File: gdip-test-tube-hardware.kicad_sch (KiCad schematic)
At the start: 13 parts, among them J1 USB_B, J2 USB_B, J3 Conn_01x06, J4 Conn_01x06, J5 Conn_01x06, U1 ESP32-S3-WROOM-1-N16R2, U2 AMS1117-3.3, U3 CP2102N-Axx-xQFN28, U4 USBLC6-2SC6, U5 USBLC6-2SC6

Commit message: Added connections for servo and finshed up usb-serial ic.
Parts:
- added C3: 1uF, symbol Device:C
- added C4: 10uF, symbol Device:C
- added R1: 22.1k, symbol Device:R
- added R2: 47.5K, symbol Device:R
- added R3: 1K, symbol Device:R
- added SW1, SW2: SW_Push, symbol Switch:SW_Push
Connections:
- net D2+_OUT: now also U3.4 (D+)
- net D2-_OUT: now also U3.5 (D-)
- net GND: now also U3.29 (GND), U3.3 (GND), C3.2, C4.2, R2.1
- net +3.3V: now reaches U3.6 (VDD)
- net +3.3V: now also U3.7 (VREGIN), C4.1, R3.1
- net at U3.8 (VBUS): now also C3.1, R1.2, R2.2
- net at U3.9 (~{RST}): now also R3.2
- net +5V: now reaches C2.1, J2.1 (VBUS), U5.5 (VBUS)
- net +5V: now also C1.1, J1.1 (VBUS), U4.5 (VBUS), R1.1
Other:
- note added: "BUTTONS"
- moved on the sheet: J3, J4, J5, U3

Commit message: Added auto prog circuit.
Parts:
- added C5: 10uF, symbol Device:C
- added C6: 0.1uF, symbol Device:C
- added J6: Screw_Terminal_01x02, symbol Connector:Screw_Terminal_01x02
- added Q1, Q2: S8050, Package_TO_SOT_THT:TO-92_Inline, symbol Transistor_BJT:S8050
- added R10, R11, R4, R5, R6, R7: 0, symbol Device:R
- added R8, R9: 10k, symbol Device:R
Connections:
- net +3.3V: now also C5.1, C6.1, R7.1
- net +5V: now also J3.1 (Pin_1), J3.2 (Pin_2), J3.3 (Pin_3), J3.4 (Pin_4), J3.5 (Pin_5), J3.6 (Pin_6)
- net GND: now also J5.1 (Pin_1), J5.2 (Pin_2), J5.3 (Pin_3), J5.4 (Pin_4), J5.5 (Pin_5), J5.6 (Pin_6), U1.1 (GND), U1.40 (GND), U1.41_1 (GND), U1.41_2 (GND), U1.41_3 (GND), U1.41_4 (GND), U1.41_5 (GND), U1.41_6 (GND), U1.41_7 (GND), U1.41_8 (GND), U1.41_9 (GND), C5.2, C6.2, R6.1
- net at U3.11 (~{SUSPEND}): now also R6.2
- net RTS: now reaches U3.24 (~{RTS})
- net RTS: now also Q1.1 (E), R9.2
- net at U3.25 (RXD): now also R5.2
- net at U3.26 (TXD): now also R4.2
- net DTR: now reaches U3.28 (~{DTR})
- net DTR: now also Q2.3 (C), R8.2
- net at U1.2 (3V3): now also R7.2
- net U0RXD: now reaches U1.36 (RXD0)
- net U0RXD: now also R4.1
- net U0TXD: now reaches U1.37 (TXD0)
- net U0TXD: now also R5.1
- new net: Q1.2 (B), R8.1
- new net: Q1.3 (C), R10.2
- new net: Q2.1 (E), R11.2
- new net: Q2.2 (B), R9.1
- new net CHIP_PU: R10.1
- new net GPIO0: R11.1
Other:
- note added: "MCU Power (3.3V)"
- note added: "Motor Supply (5V)"
- note added: "Power Pin Headers"
- note added: "USB"
- moved on the sheet: C3, C4, J3, J4, J5, R1, R2, R3, SW1, SW2, U1, U2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

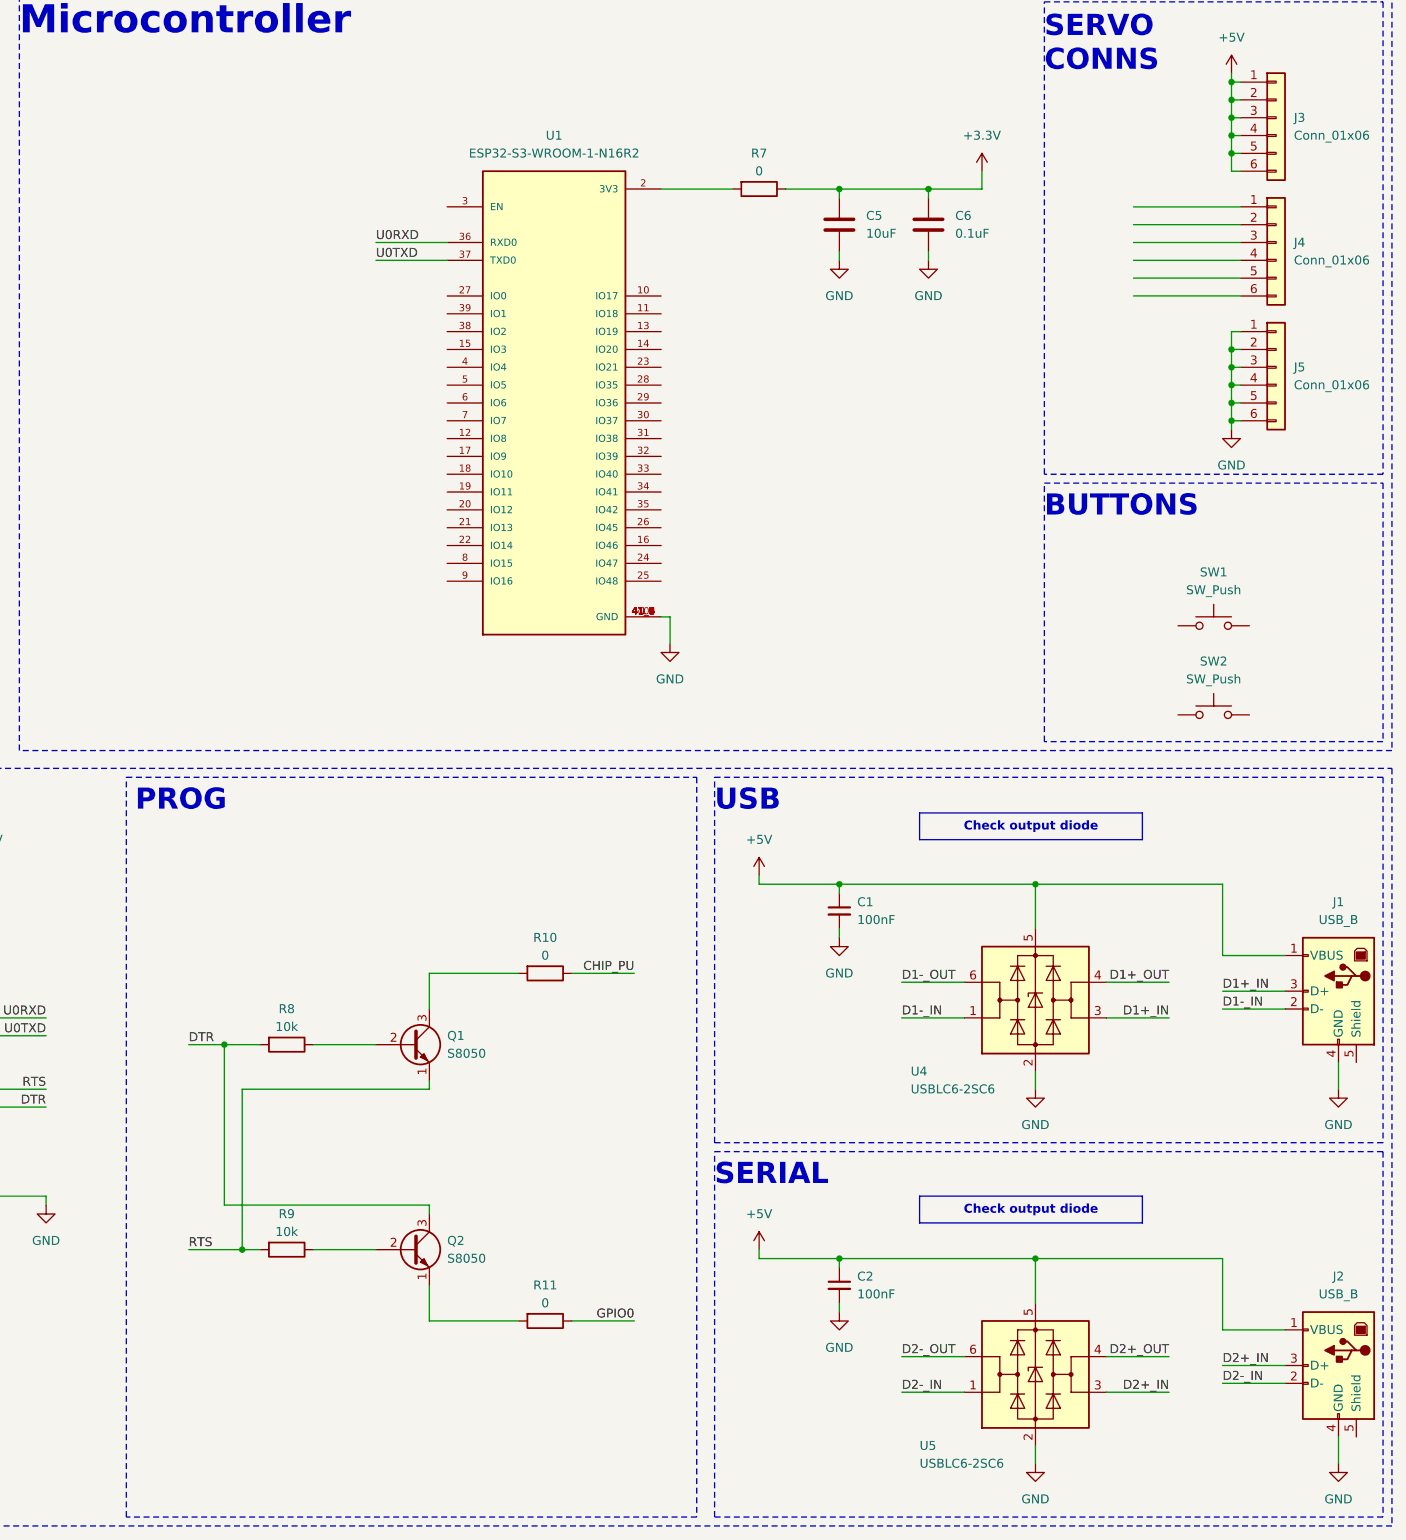
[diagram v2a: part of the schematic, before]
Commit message: Added pinout and connect pwm to servo pin header.
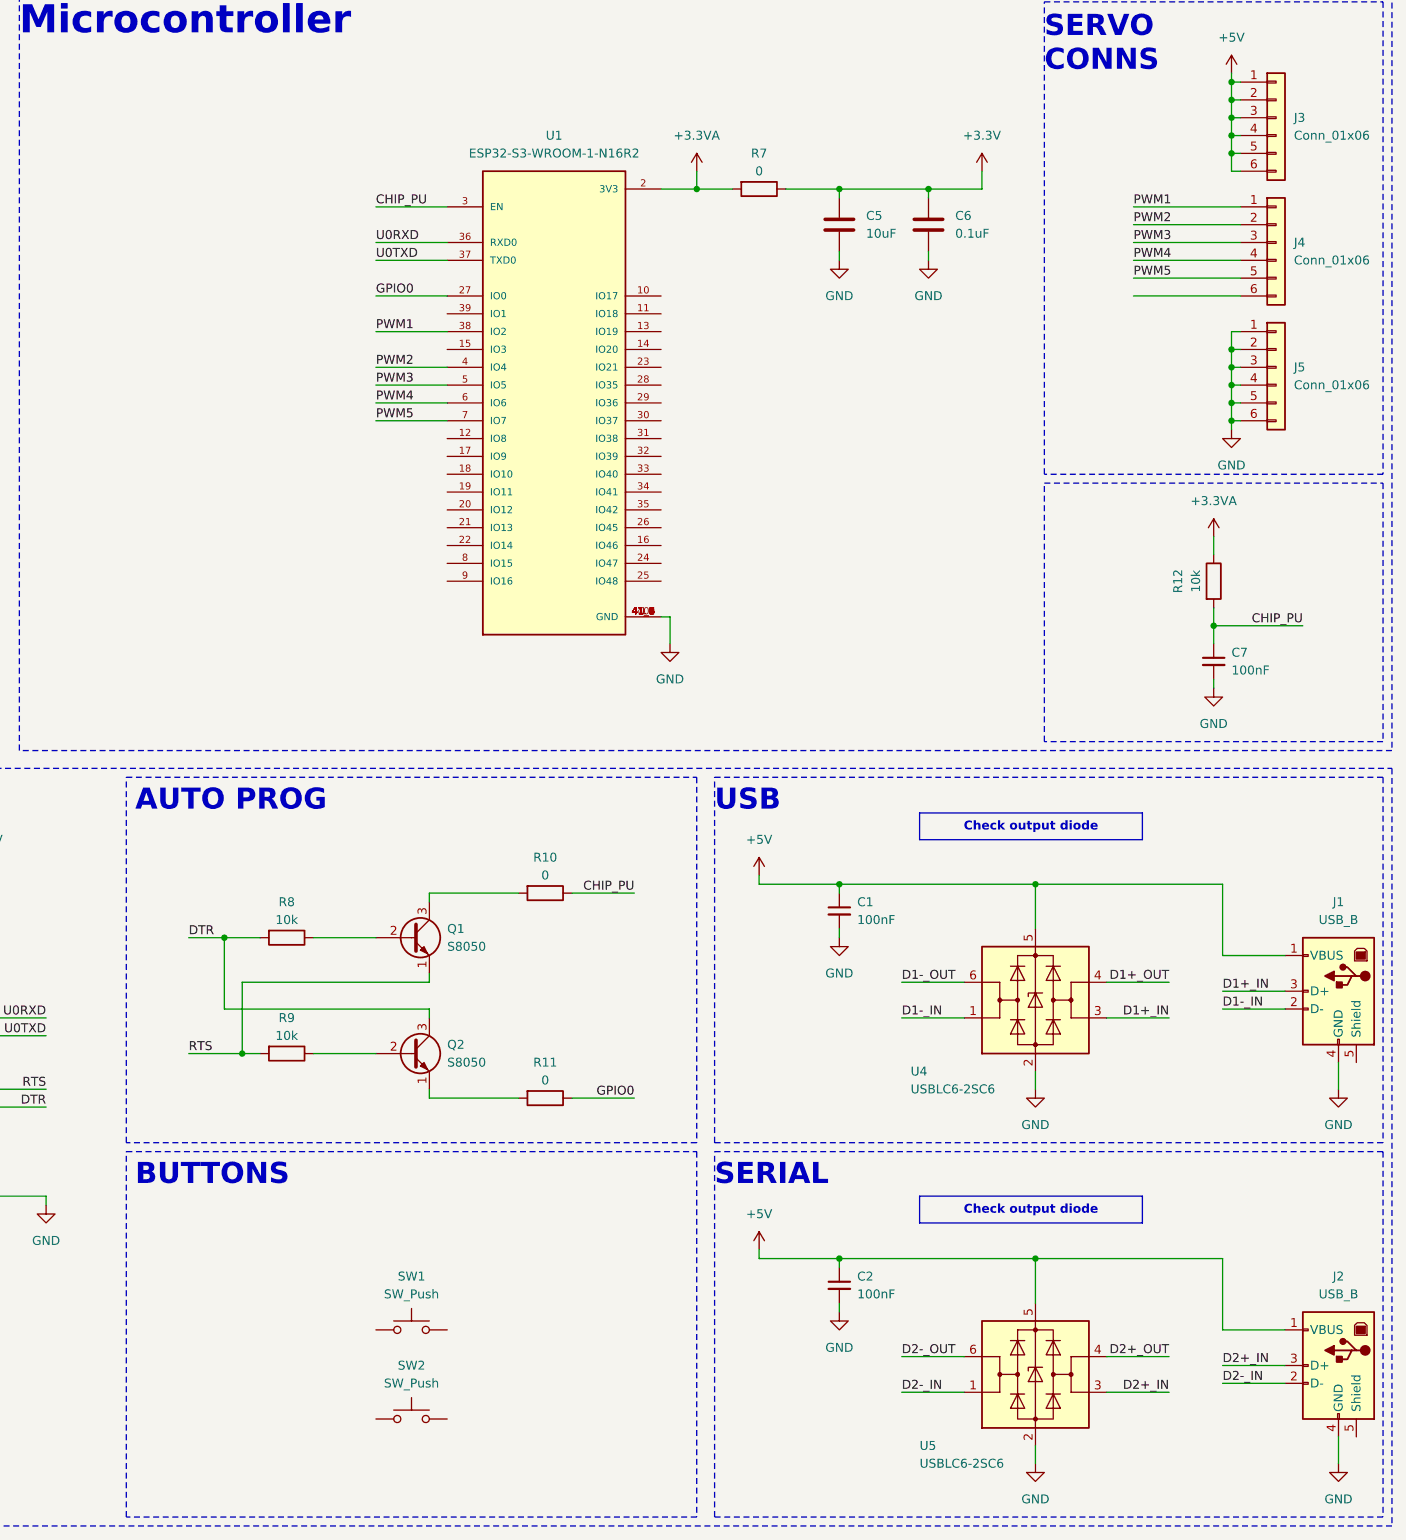
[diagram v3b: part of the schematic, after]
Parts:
- added C7: 100nF, symbol Device:C_Small
- added R12: 10k, symbol Device:R
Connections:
- net CHIP_PU: now also U1.3 (EN), C7.1, R12.2
- net GND: now also C7.2
- net GPIO0: now also U1.27 (IO0)
- net +3.3VA: now reaches R7.2, U1.2 (3V3)
- net +3.3VA: now also R12.1
- net PWM1: now reaches J4.1 (Pin_1)
- net PWM1: now also U1.38 (IO2)
- net PWM2: now reaches J4.2 (Pin_2)
- net PWM2: now also U1.4 (IO4)
- net PWM3: now reaches J4.3 (Pin_3)
- net PWM3: now also U1.5 (IO5)
- net PWM4: now reaches J4.4 (Pin_4)
- net PWM4: now also U1.6 (IO6)
- net PWM5: now reaches J4.5 (Pin_5)
- net PWM5: now also U1.7 (IO7)
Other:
- note added: "AUTO PROG"
- note removed: "PROG"
- moved on the sheet: Q1, Q2, R10, R11, R8, R9, SW1, SW2

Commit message: Finshed switch cricuit for prog.
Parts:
- removed BZ1: Buzzer, symbol Device:Buzzer
- added C8, C9: 0.1uF, symbol Device:C_Small
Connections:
- net CHIP_PU: now also SW2.2, C9.2
- net GND: now also SW1.1, SW2.1, C8.1, C9.1
- net GPIO0: now also SW1.2, C8.2
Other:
- moved on the sheet: C1, C2, C3, C4, J1, J2, Q1, Q2, R1, R10, R11, R2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

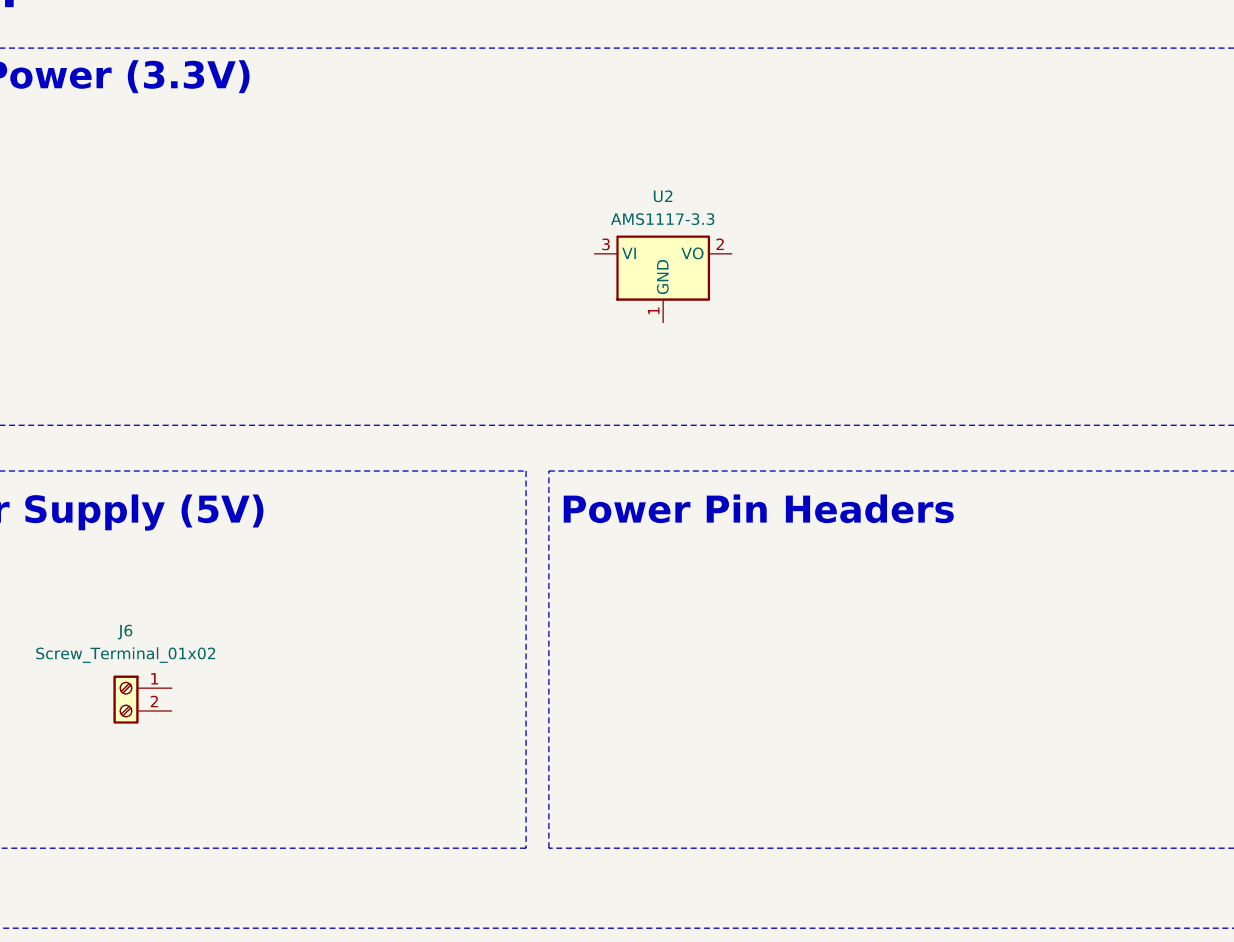
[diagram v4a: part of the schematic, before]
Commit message: Added caps for 3.3V reg and added nets for motor power supply.
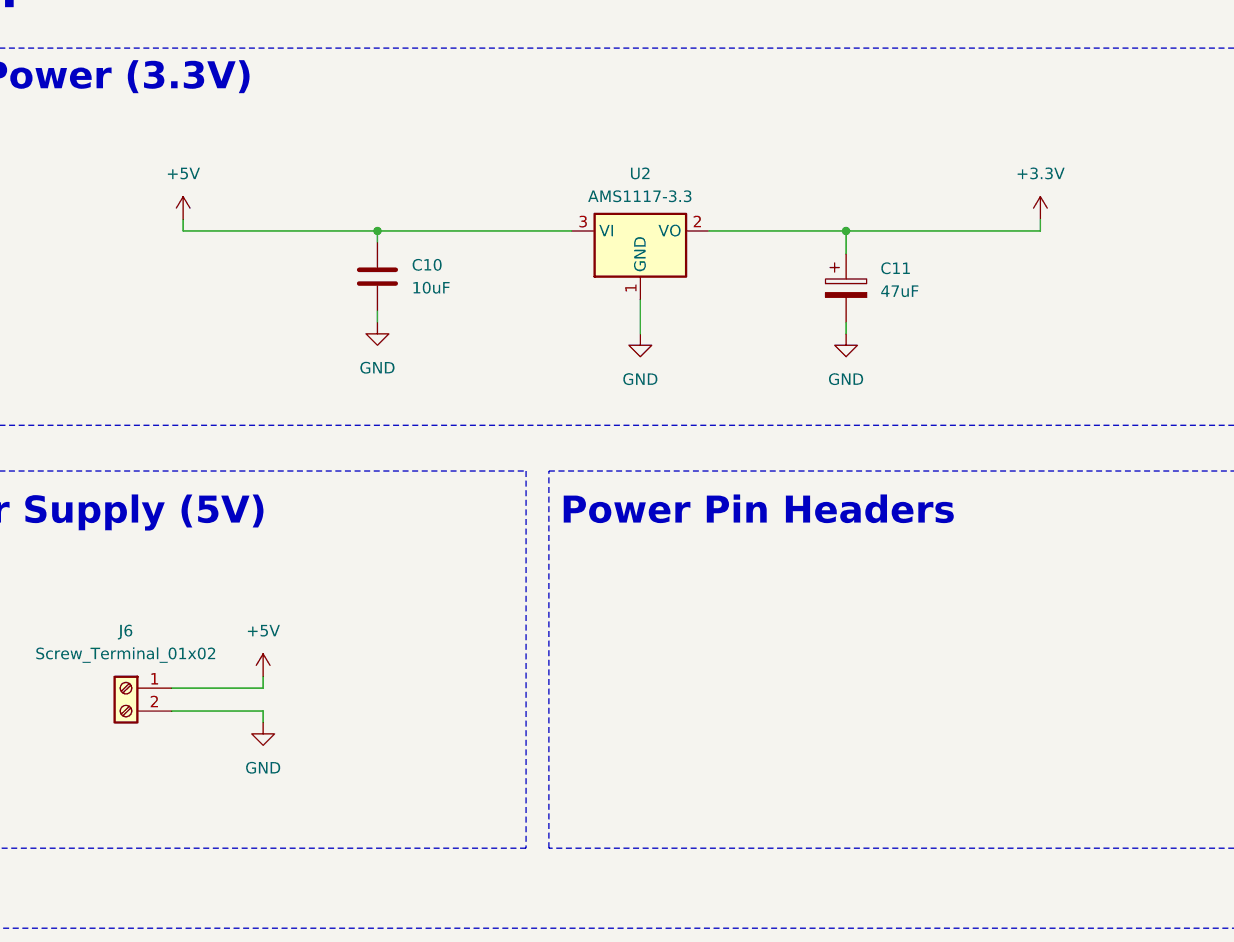
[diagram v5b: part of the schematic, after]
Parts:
- added C10: 10uF, symbol Device:C
- added C11: 47uF, symbol Device:C_Polarized
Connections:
- net +3.3V: now also U2.2 (VO), C11.1
- net +5V: now also J6.1 (Pin_1), U2.3 (VI), C10.1
- net GND: now also J6.2 (Pin_2), U2.1 (GND), C10.2, C11.2
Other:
- moved on the sheet: U2
